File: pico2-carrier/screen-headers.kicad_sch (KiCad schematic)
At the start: 8 parts, among them J1 SCREEN_HDR, J2 DO0180FMST08, J3 Ext_Pwr_Rail

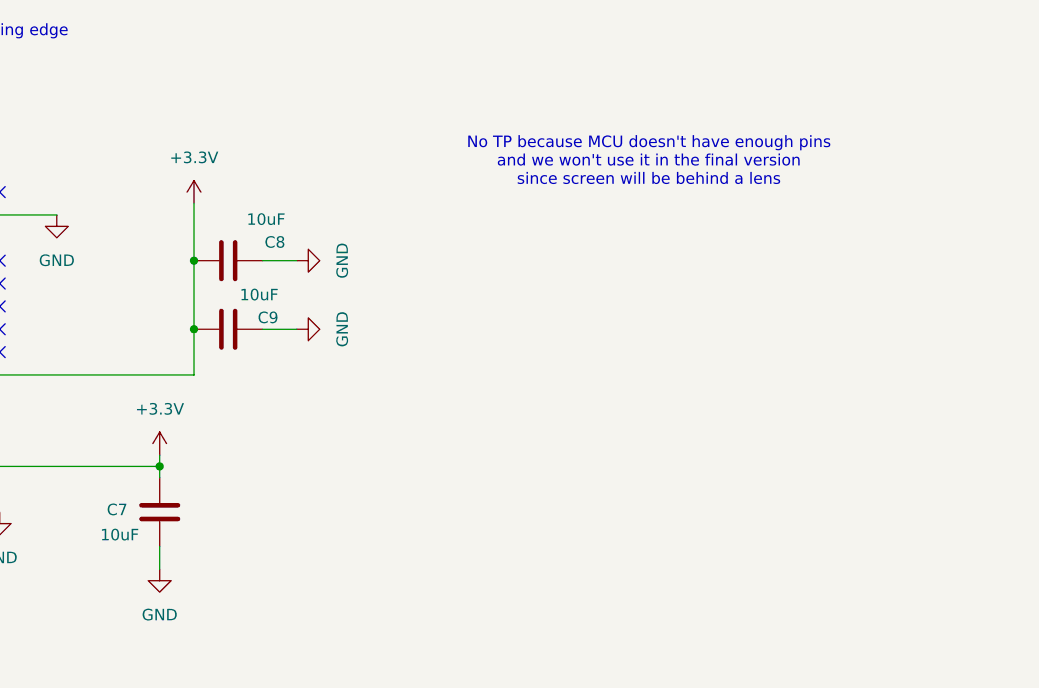
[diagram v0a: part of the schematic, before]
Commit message: finish routing - DRC ok
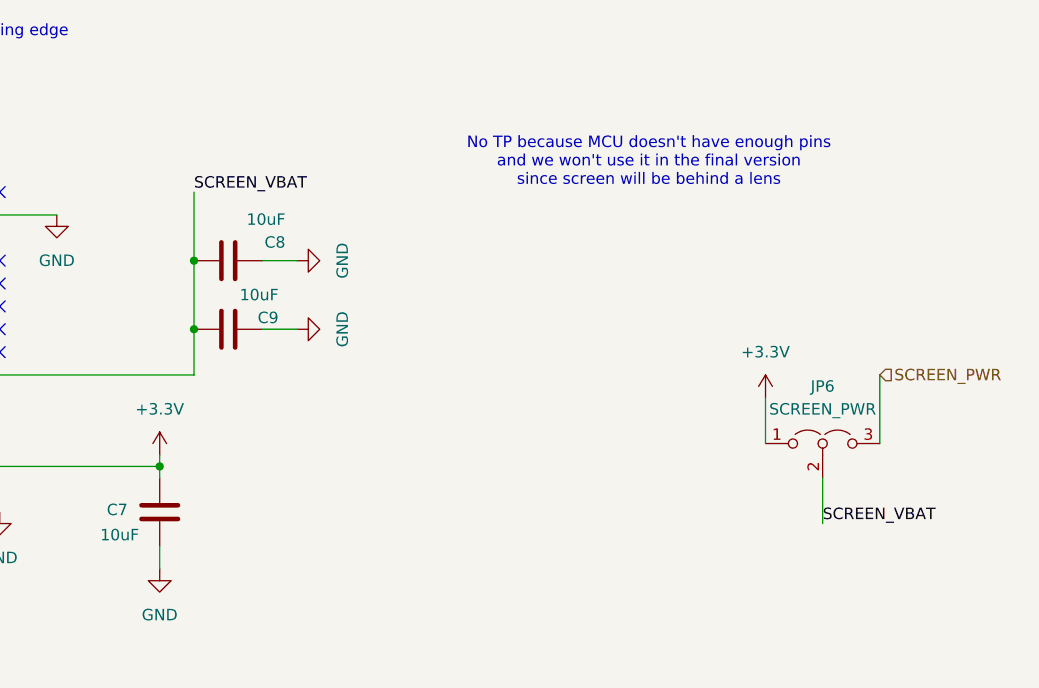
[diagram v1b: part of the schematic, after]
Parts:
- added JP6: SCREEN_PWR, Connector_PinHeader_2.54mm:PinHeader_1x03_P2.54mm_Vertical, symbol Jumper:Jumper_3_Open
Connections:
- net +3.3V: now also JP6.1 (A); no longer C8.1, C9.1, J2.18 (VBAT), J2.20 (VBAT)
- new net SCREEN_PWR: JP6.3 (B)
- new net SCREEN_VBAT: C8.1, C9.1, J2.18 (VBAT), J2.20 (VBAT), JP6.2 (C)
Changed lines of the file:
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@@
+	(wire
+		(pts
+			(xy 217.17 62.23) (xy 217.17 67.31)
+		)
+		(stroke
+			(width 0)
+			(type default)
+		)
+	)
 	(wire
 		(pts
@@
 	(wire
 		(pts
-			(xy 153.67 40.64) (xy 153.67 46.99)
+			(xy 153.67 39.37) (xy 153.67 46.99)
 		)
 		(stroke
@@
 	(wire
 		(pts
+			(xy 229.87 59.69) (xy 229.87 67.31)
+		)
+		(stroke
+			(width 0)
+			(type default)
+		)
+	)
+	(wire
+		(pts
 			(xy 153.67 46.99) (xy 153.67 54.61)
 		)
@@
 		(pts
 			(xy 139.7 138.43) (xy 144.78 138.43)
+		)
+		(stroke
+			(width 0)
+			(type default)
+		)
+	)
+	(wire
+		(pts
+			(xy 223.52 71.12) (xy 223.52 76.2)
 		)
 		(stroke
@@
 		)
 	)
+	(label "SCREEN_VBAT"
+		(at 153.67 39.37 0)
+		(fields_autoplaced yes)
+		(effects
+			(font
+				(size 1.27 1.27)
+			)
+			(justify left bottom)
+		)
+	)
+	(label "SCREEN_VBAT"
+		(at 223.52 76.2 0)
+		(fields_autoplaced yes)
+		(effects
+			(font
+				(size 1.27 1.27)
+			)
+			(justify left bottom)
+		)
+	)
 	(label "TP_INT"
 		(at 130.81 52.07 180)
@@
 		(shape input)
 		(at 114.3 134.62 0)
+		(fields_autoplaced yes)
+		(effects
+			(font
+				(size 1.27 1.27)
+			)
+			(justify left)
+		)
+	)
+	(hierarchical_label "SCREEN_PWR"
+		(shape input)
+		(at 229.87 59.69 0)
 		(fields_autoplaced yes)
 		(effects
@@
 		(lib_name "+3.3V_1")
 		(lib_id "power:+3.3V")
-		(at 153.67 40.64 0)
+		(at 217.17 62.23 0)
+		(mirror y)
 		(unit 1)
 		(exclude_from_sim no)
@@
 		(on_board yes)
 		(dnp no)
-		(fields_autoplaced yes)
-		(property "Reference" "#PWR045"
-			(at 153.67 44.45 0)
+		(property "Reference" "#PWR062"
+			(at 217.17 66.04 0)
 			(effects
 				(font
@@
 		)
 		(property "Value" "+3.3V"
-			(at 153.67 35.56 0)
+			(at 217.17 57.15 0)
 			(effects
 				(font
@@
 		)
 		(property "Footprint" ""
-			(at 153.67 40.64 0)
+			(at 217.17 62.23 0)
 			(effects
 				(font
@@
 		)
 		(property "Datasheet" ""
-			(at 153.67 40.64 0)
+			(at 217.17 62.23 0)
 			(effects
 				(font
@@
 		)
 		(property "Description" "Power symbol creates a global label with name \"+3.3V\""
-			(at 153.67 40.64 0)
+			(at 217.17 62.23 0)
 			(effects
 				(font
@@
 			(project "pico2-carrier"
 				(path "/4204b4ad-0ae5-4a8a-a079-fb4cf2b0ed9e/8ff523db-30f4-4441-afe8-9b6de18f8394"
-					(reference "#PWR045")
+					(reference "#PWR062")
 					(unit 1)
 				)
@@
 					(unit 1)
 				)
+			)
+		)
+	)
+	(symbol
+		(lib_id "Jumper:Jumper_3_Open")
+		(at 223.52 67.31 0)
+		(unit 1)
+		(exclude_from_sim yes)
+		(in_bom no)
+		(on_board yes)
+		(dnp no)
+		(fields_autoplaced yes)
+		(property "Reference" "JP6"
+			(at 223.52 60.96 0)
+			(effects
+				(font
+					(size 1.27 1.27)
+				)
+			)
+		)
+		(property "Value" "SCREEN_PWR"
+			(at 223.52 63.5 0)
+			(effects
+				(font
+					(size 1.27 1.27)
+				)
+			)
+		)
+		(property "Footprint" "Connector_PinHeader_2.54mm:PinHeader_1x03_P2.54mm_Vertical"
+			(at 223.52 67.31 0)
+			(effects
+				(font
+					(size 1.27 1.27)
+				)
+				(hide yes)
+			)
+		)
+		(property "Datasheet" "~"
+			(at 223.52 67.31 0)
+			(effects
+				(font
+					(size 1.27 1.27)
+				)
+				(hide yes)
+			)
+		)
+		(property "Description" "Jumper, 3-pole, both open"
+			(at 223.52 67.31 0)
+			(effects
+				(font
+					(size 1.27 1.27)
+				)
+				(hide yes)
+			)
+		)
+		(pin "2"
+		)
+		(pin "1"
+		)
+		(pin "3"
+		)
+		(instances
+			(project "pico2-carrier"
+				(path "/4204b4ad-0ae5-4a8a-a079-fb4cf2b0ed9e/8ff523db-30f4-4441-afe8-9b6de18f8394"
+					(reference "JP6")
+					(unit 1)
+				)

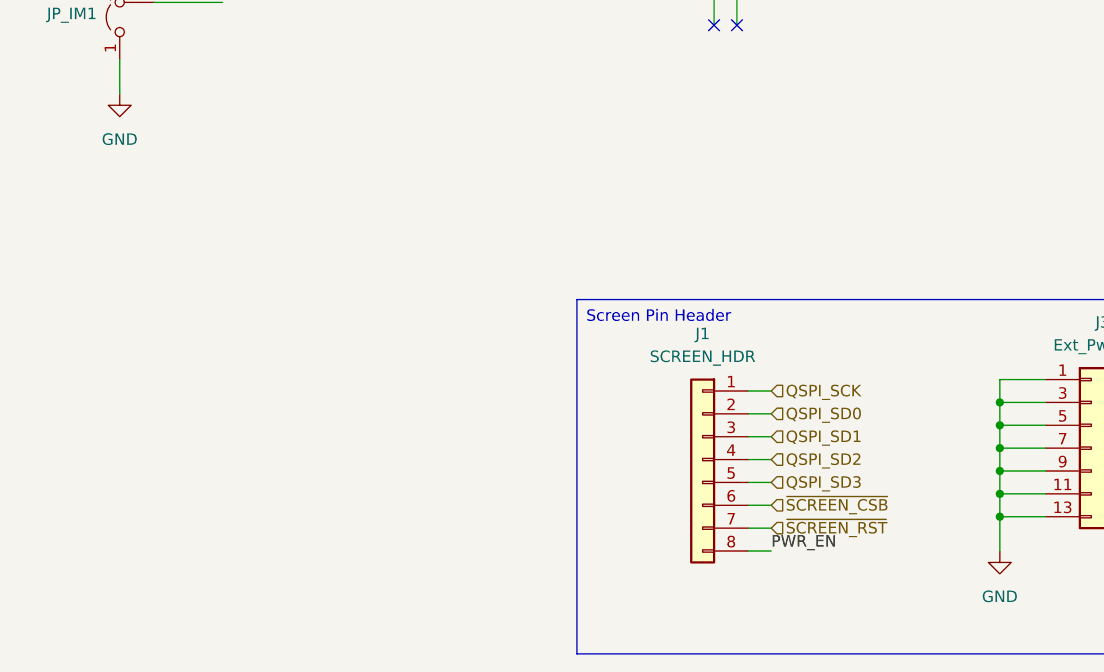
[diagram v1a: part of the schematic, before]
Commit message: carrier: new pcb degisn for better screen placement
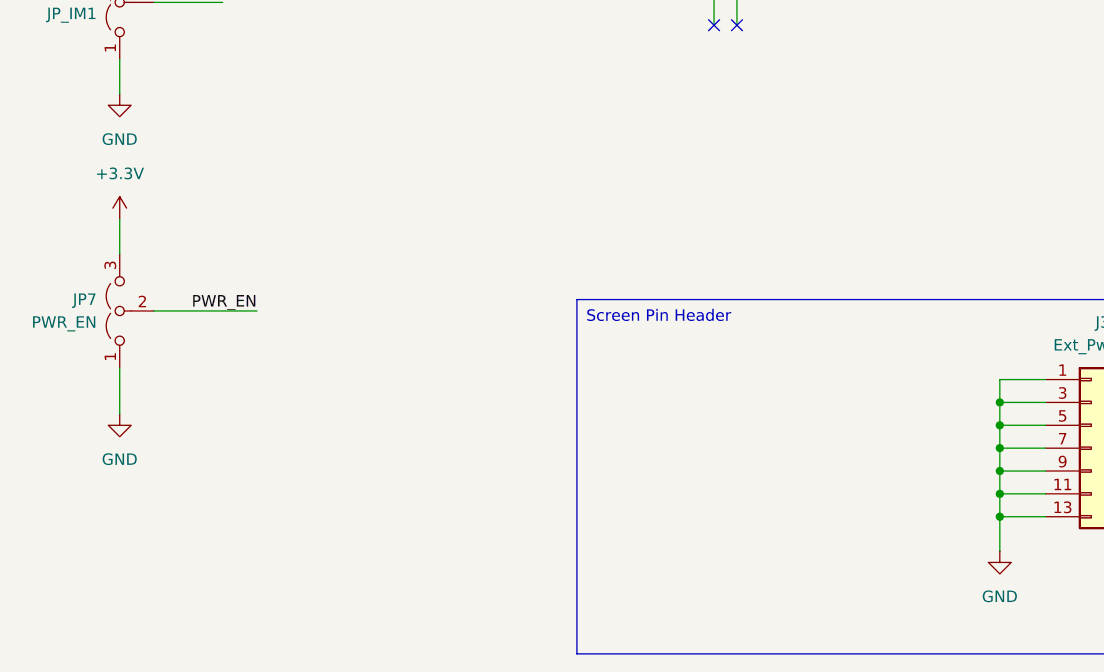
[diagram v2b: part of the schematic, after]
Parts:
- removed J1: SCREEN_HDR, Connector_PinHeader_2.54mm:PinHeader_1x08_P2.54mm_Vertical, symbol Connector_Generic:Conn_01x08
- added JP7: PWR_EN, Jumper:SolderJumper-3_P1.3mm_Open_Pad1.0x1.5mm, symbol Jumper:Jumper_3_Open
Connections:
- net +3.3V: now also JP7.3 (B)
- net GND: now also JP7.1 (A)
- net PWR_EN: now also JP7.2 (C)

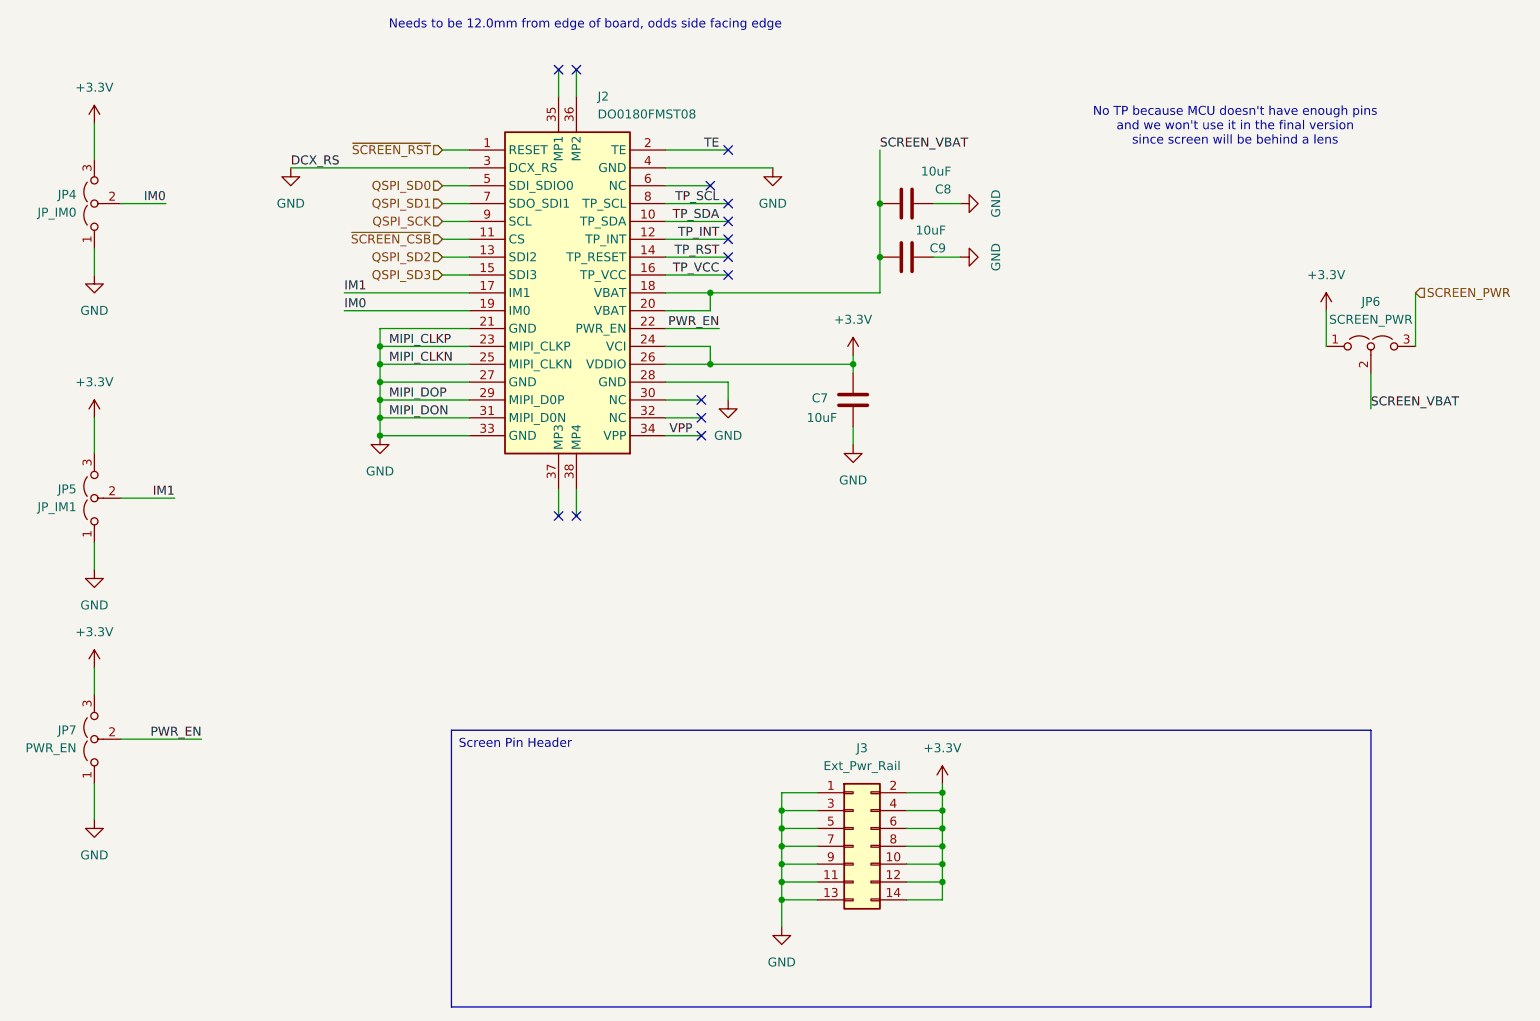
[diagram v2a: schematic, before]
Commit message: carrier: add some test points and default jumper connections
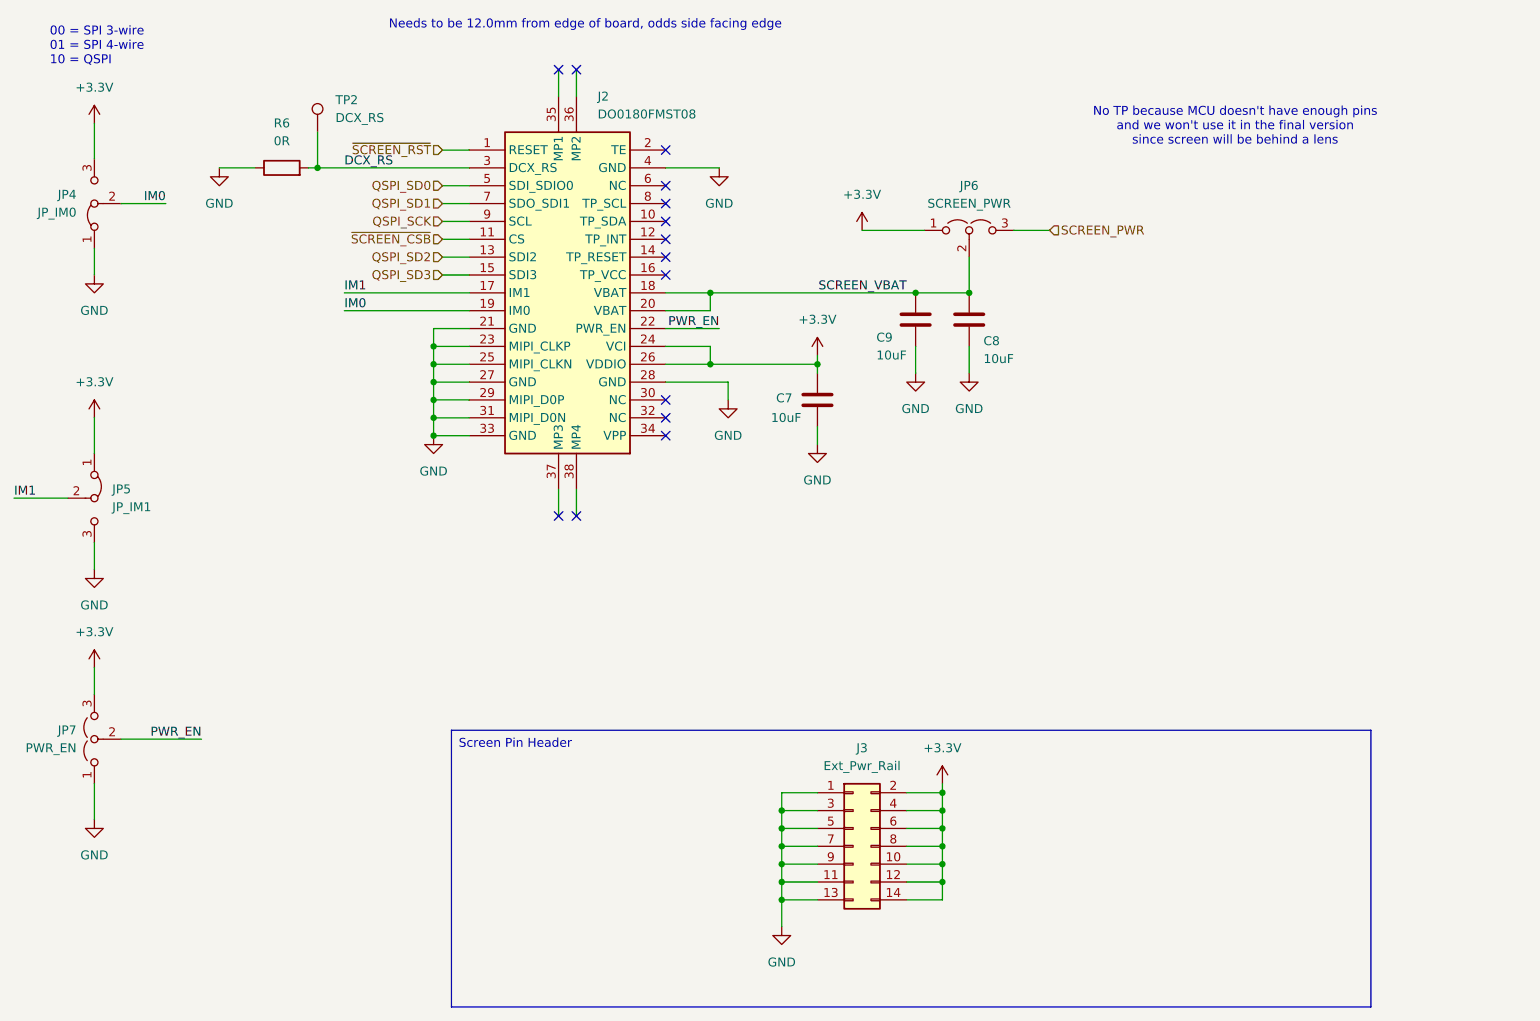
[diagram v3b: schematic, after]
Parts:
- added R6: 0R, Capacitor_SMD:C_0402_1005Metric, symbol Device:R
- added TP2: DCX_RS, Connector_PinHeader_2.54mm:PinHeader_1x01_P2.54mm_Vertical, symbol Connector:TestPoint
- JP4, JP5: symbol Jumper:Jumper_3_Open -> Jumper:Jumper_3_Bridged12
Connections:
- net +3.3V: now also JP5.1 (A); no longer JP5.3 (B)
- net GND: now also JP5.3 (B), R6.1; no longer J2.3 (DCX_RS), JP5.1 (A)
- net TE: no longer names the net of J2.2 (TE)
- net TP_INT: no longer names the net of J2.12 (TP_INT)
- net TP_RST: no longer names the net of J2.14 (TP_RESET)
- net TP_SCL: no longer names the net of J2.8 (TP_SCL)
- net TP_SDA: no longer names the net of J2.10 (TP_SDA)
- net TP_VCC: no longer names the net of J2.16 (TP_VCC)
- net VPP: no longer names the net of J2.34 (VPP)
- new net DCX_RS: J2.3 (DCX_RS), R6.2, TP2.1
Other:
- note added: "00 = SPI 3-wire 01 = SPI 4-wire 10 = QSPI"
- moved on the sheet: C7, C8, C9, JP6

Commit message: carrier: add hardware button debounce
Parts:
- JP7: footprint Jumper:SolderJumper-3_P1.3mm_Open_Pad1.0x1.5mm -> Connector_PinHeader_2.54mm:PinHeader_1x03_P2.54mm_Vertical
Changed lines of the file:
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@@
 			)
 		)
-		(property "Footprint" "Jumper:SolderJumper-3_P1.3mm_Open_Pad1.0x1.5mm"
+		(property "Footprint" "Connector_PinHeader_2.54mm:PinHeader_1x03_P2.54mm_Vertical"
 			(at 41.91 123.19 0)
 			(effects

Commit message: carrier: add 3.3V zone, start tidying buttons, update caps to 0603
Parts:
- C7, C8, C9: footprint Capacitor_SMD:C_0402_1005Metric -> Capacitor_SMD:C_0603_1608Metric
- JP4, JP5: footprint Jumper:SolderJumper-3_P1.3mm_Open_Pad1.0x1.5mm -> Jumper:SolderJumper-3_P1.3mm_Bridged12_Pad1.0x1.5mm
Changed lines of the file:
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@@
 			)
 		)
-		(property "Footprint" "Capacitor_SMD:C_0402_1005Metric"
+		(property "Footprint" "Capacitor_SMD:C_0603_1608Metric"
 			(at 159.7152 67.31 0)
 			(effects
@@
 			)
 		)
-		(property "Footprint" "Jumper:SolderJumper-3_P1.3mm_Open_Pad1.0x1.5mm"
+		(property "Footprint" "Jumper:SolderJumper-3_P1.3mm_Bridged12_Pad1.0x1.5mm"
 			(at 41.91 46.99 0)
 			(effects
@@
 			)
 		)
-		(property "Footprint" "Capacitor_SMD:C_0402_1005Metric"
+		(property "Footprint" "Capacitor_SMD:C_0603_1608Metric"
 			(at 167.3352 67.31 0)
 			(effects
@@
 			)
 		)
-		(property "Footprint" "Capacitor_SMD:C_0402_1005Metric"
+		(property "Footprint" "Capacitor_SMD:C_0603_1608Metric"
 			(at 143.8148 78.74 0)
 			(effects
@@
 			)
 		)
-		(property "Footprint" "Jumper:SolderJumper-3_P1.3mm_Open_Pad1.0x1.5mm"
+		(property "Footprint" "Jumper:SolderJumper-3_P1.3mm_Bridged12_Pad1.0x1.5mm"
 			(at 41.91 88.9 0)
 			(effects
